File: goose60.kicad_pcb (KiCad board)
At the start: 2 copper layers, 285 x 94.6 mm, 188 parts, among them J1 Debugger, J2 USART, J3 SPI, J4 USB_C_Receptacle_USB2.0, Q1 Q_NMOS_GSD, SW1 SW_Push, SW10 SW_Push, SW11 SW_Push, SW14 SW_Push, SW15 SW_Push, SW16 SW_Push, SW18 SW_Push, SW2 SW_Push, SW20 SW_Push, SW21 SW_Push, SW22 SW_Push, SW23 SW_Push, SW24 SW_Push, SW25 SW_Push, SW26 SW_Push, SW27 SW_Push, SW28 SW_Push, SW29 SW_Push, SW3 SW_Push, SW30 SW_Push, SW31 SW_Push, SW32 SW_Push, SW35 SW_Push, SW36 SW_Push, SW37 SW_Push, SW38 SW_Push, SW39 SW_Push, SW40 SW_Push, SW41 SW_Push, SW42 SW_Push, SW43 SW_Push, SW44 SW_Push, SW45 SW_Push, SW46 SW_Push, SW47 SW_Push, SW48 SW_Push, SW49 SW_Push, SW5 SW_Push, SW50 SW_Push, SW51 SW_Push, SW52 SW_Push, SW53 SW_Push, SW54 SW_Push, SW56 SW_Push, SW58 SW_Push, SW59 SW_Push, SW60 SW_Push, SW61 SW_Push, SW62 SW_Push, SW65 SW_Push, SW66 SW_Push, SW67 SW_Push, SW68 SW_Push, SW69 SW_Push, SW7 SW_Push, SW71 SW_Push, SW73 SW_Push, SW74 SW_Push, SW75 SW_Push, SW76 SW_Push, SW78 SW_Push, SW79 SW_Push, SW80 SW_Push, SW82 SW_Push, SW84 SW_Push, SW86 SW_Push, SW9 SW_Push, U1 STM32F103CBTx, U2 LM317_SOT-223, U3 USBLC6-2SC6, X1 Crystal_GND24

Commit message: fix usb type-c location
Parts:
- moved H7 0.95 mm to (82.0, 73.9)
- moved J4 0.85 mm to (80.7, 67.3)
- moved H8 0.81 mm to (79.3, 73.8)
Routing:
- net Net-(J4-PadA7): track 31.0 -> 30.0 mm
- net row1: track 353.6 -> 354.5 mm
- net Net-(J4-PadB5): track 9.05 -> 9.90 mm
- net Net-(J4-PadA5): track 8.58 -> 9.43 mm
- net Net-(J4-PadA6): track 29.9 -> 29.2 mm

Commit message: change Diode direction and update PR #1 footprint
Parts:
- removed D69: 6.3V/100V, Diode_SMD:D_0603_1608Metric
- added C12: 100uF/16v, Capacitor_SMD:C_1206_3216Metric, B.Cu at (121.3, 85.6)
- added C13: 1uF/16v, Capacitor_SMD:C_0603_1608Metric, B.Cu at (124.8, 84.5)
- added C14: 1uF/16v, Capacitor_SMD:C_0603_1608Metric, B.Cu at (142.3, 85.3)
- added D13: 1N4148, Diode_SMD:D_0805_2012Metric, B.Cu at (139.1, 84.4)
- added R23: 100K/5%, Resistor_SMD:R_0603_1608Metric, B.Cu at (228.6, 144.9)
- added R27: 100K/5%, Resistor_SMD:R_0603_1608Metric, B.Cu at (241.1, 144.9)
- added R28: 10K/5%, Resistor_SMD:R_0603_1608Metric, B.Cu at (117.8, 83.0)
- C1, C2: value 22pF -> 22pF/50V
- C10: footprint Capacitor_SMD:C_0603_1608Metric -> Capacitor_SMD:C_1206_3216Metric
- C3: value 1uF -> 1uF/16V
- C4, C5, C6, C7: value 100nF -> 100nF/16V
- C9: footprint Capacitor_SMD:C_0603_1608Metric -> Capacitor_SMD:C_0805_2012Metric
- D10, D11, D12, D14, D15, D16, D17, D18, D19, D20, D21, D22, D23, D24, D25, D26, D27, D28, D29, D30, D31, D32, D33, D34, D35, D36, D37, D38, D39, D4, D40, D41, D42, D43, D44, D45, D46, D47, D49, D5, D50, D51, D52, D53, D54, D55, D56, D57, D58, D59, D6, D60, D61, D62, D63, D64, D65, D66, D67, D68, D7, D8, D9: footprint Diode_SMD:D_0603_1608Metric -> Diode_SMD:D_0805_2012Metric
- D70: value 1SS355TE -> 1N4148; footprint Diode_SMD:D_0603_1608Metric -> Diode_SMD:D_0805_2012Metric
- R1, R15, R16, R17, R18, R19, R2, R20, R21, R22, R7, R8: value 10K -> 10K/5%
- R10, R9: value 22 -> 22R/5%
- R11: value 1.5K -> 1.5K/5%
- R12, R13, R14: value 0 -> 0R/5%
- R24, R25: value 5.1K -> 5.1K/5%
- R26: value 10K -> 100R/5%
- R3: value 300 -> 330R/5%
- moved C10 1.57 mm to (140.6, 87.8)
- moved D5 0.95 mm to (77.6, 127.4), turned to 180 degrees
- moved D16 0.65 mm to (117.0, 103.1), turned to 180 degrees
- moved D20 0.44 mm to (132.1, 102.3), turned to 90 degrees
- moved D70 0.36 mm to (127.3, 88.0)
- moved D10 0.36 mm to (83.6, 75.8), turned to -90 degrees
- moved D26 0.35 mm to (145.8, 129.3), turned to -90 degrees
- moved D31 0.35 mm to (163.6, 129.3), turned to -90 degrees
- moved D35 0.35 mm to (183.4, 129.3), turned to -90 degrees
- moved D39 0.35 mm to (201.8, 129.3), turned to -90 degrees
- moved D43 0.35 mm to (220.8, 129.3), turned to -90 degrees
- moved D47 0.35 mm to (239.8, 129.3), turned to -90 degrees
- moved D53 0.35 mm to (259.6, 129.3), turned to -90 degrees
- moved D58 0.35 mm to (278.3, 129.3), turned to -90 degrees
- moved D18 0.33 mm to (105.0, 129.3), turned to -90 degrees
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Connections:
- D10 pad 1: Net-(D10-Pad1) -> row1
- D10 pad 2: row1 -> Net-(D10-Pad2)
- D11 pad 1: Net-(D11-Pad1) -> row2
- D11 pad 2: row2 -> Net-(D11-Pad2)
- D12 pad 1: Net-(D12-Pad1) -> row3
- D12 pad 2: row3 -> Net-(D12-Pad2)
- D14 pad 1: Net-(D14-Pad1) -> row5
- D14 pad 2: row5 -> Net-(D14-Pad2)
- D15 pad 1: Net-(D15-Pad1) -> row1
- D15 pad 2: row1 -> Net-(D15-Pad2)
- D16 pad 1: Net-(D16-Pad1) -> row2
- D16 pad 2: row2 -> Net-(D16-Pad2)
- D17 pad 1: Net-(D17-Pad1) -> row3
- D17 pad 2: row3 -> Net-(D17-Pad2)
- D18 pad 1: Net-(D18-Pad1) -> row4
- D18 pad 2: row4 -> Net-(D18-Pad2)
- D19 pad 1: Net-(D19-Pad1) -> row1
- D19 pad 2: row1 -> Net-(D19-Pad2)
- D20 pad 1: Net-(D20-Pad1) -> row2
- D20 pad 2: row2 -> Net-(D20-Pad2)
- D21 pad 1: Net-(D21-Pad1) -> row3
- D21 pad 2: row3 -> Net-(D21-Pad2)
- D22 pad 1: Net-(D22-Pad1) -> row4
- D22 pad 2: row4 -> Net-(D22-Pad2)
- D23 pad 1: Net-(D23-Pad1) -> row1
- D23 pad 2: row1 -> Net-(D23-Pad2)
- D24 pad 1: Net-(D24-Pad1) -> row2
- D24 pad 2: row2 -> Net-(D24-Pad2)
- D25 pad 1: Net-(D25-Pad1) -> row3
- D25 pad 2: row3 -> Net-(D25-Pad2)
- D26 pad 1: Net-(D26-Pad1) -> row4
- D26 pad 2: row4 -> Net-(D26-Pad2)
- D27 pad 1: Net-(D27-Pad1) -> row5
- D27 pad 2: row5 -> Net-(D27-Pad2)
- D28 pad 1: Net-(D28-Pad1) -> row1
- D28 pad 2: row1 -> Net-(D28-Pad2)
- D29 pad 1: Net-(D29-Pad1) -> row2
- D29 pad 2: row2 -> Net-(D29-Pad2)
- D30 pad 1: Net-(D30-Pad1) -> row3
- D30 pad 2: row3 -> Net-(D30-Pad2)
- D31 pad 1: Net-(D31-Pad1) -> row4
- D31 pad 2: row4 -> Net-(D31-Pad2)
- D32 pad 1: Net-(D32-Pad1) -> row1
- D32 pad 2: row1 -> Net-(D32-Pad2)
- D33 pad 1: Net-(D33-Pad1) -> row2
- D33 pad 2: row2 -> Net-(D33-Pad2)
- D34 pad 1: Net-(D34-Pad1) -> row3
- D34 pad 2: row3 -> Net-(D34-Pad2)
- D35 pad 1: Net-(D35-Pad1) -> row4
- D35 pad 2: row4 -> Net-(D35-Pad2)
- D37 pad 1: Net-(D37-Pad1) -> row2
- D37 pad 2: row2 -> Net-(D37-Pad2)
- D38 pad 1: Net-(D38-Pad1) -> row3
- D38 pad 2: row3 -> Net-(D38-Pad2)
- D39 pad 1: Net-(D39-Pad1) -> row4
- D39 pad 2: row4 -> Net-(D39-Pad2)
- D4 pad 1: Net-(D4-Pad1) -> row3
- D4 pad 2: row3 -> Net-(D4-Pad2)
- D40 pad 1: Net-(D40-Pad1) -> row1
- D40 pad 2: row1 -> Net-(D40-Pad2)
- D41 pad 1: Net-(D41-Pad1) -> row2
- D41 pad 2: row2 -> Net-(D41-Pad2)
- D42 pad 1: Net-(D42-Pad1) -> row3
- D42 pad 2: row3 -> Net-(D42-Pad2)
- D43 pad 1: Net-(D43-Pad1) -> row4
- D43 pad 2: row4 -> Net-(D43-Pad2)
- D44 pad 1: Net-(D44-Pad1) -> row1
- D44 pad 2: row1 -> Net-(D44-Pad2)
- D45 pad 1: Net-(D45-Pad1) -> row2
- D45 pad 2: row2 -> Net-(D45-Pad2)
- D46 pad 1: Net-(D46-Pad1) -> row3
- D46 pad 2: row3 -> Net-(D46-Pad2)
- D47 pad 1: Net-(D47-Pad1) -> row4
- D47 pad 2: row4 -> Net-(D47-Pad2)
- D49 pad 1: Net-(D49-Pad1) -> row5
- D49 pad 2: row5 -> Net-(D49-Pad2)
- D5 pad 1: Net-(D5-Pad1) -> row4
- D5 pad 2: row4 -> Net-(D5-Pad2)
- D50 pad 1: Net-(D50-Pad1) -> row1
- D50 pad 2: row1 -> Net-(D50-Pad2)
- D51 pad 1: Net-(D51-Pad1) -> row2
- D51 pad 2: row2 -> Net-(D51-Pad2)
- D52 pad 1: Net-(D52-Pad1) -> row3
- D52 pad 2: row3 -> Net-(D52-Pad2)
- D53 pad 1: Net-(D53-Pad1) -> row4
- D53 pad 2: row4 -> Net-(D53-Pad2)
- D54 pad 1: Net-(D54-Pad1) -> row5
- D54 pad 2: row5 -> Net-(D54-Pad2)
- D55 pad 1: Net-(D55-Pad1) -> row1
- D55 pad 2: row1 -> Net-(D55-Pad2)
- D56 pad 1: Net-(D56-Pad1) -> row2
- D56 pad 2: row2 -> Net-(D56-Pad2)
- D57 pad 1: Net-(D57-Pad1) -> row3
- D57 pad 2: row3 -> Net-(D57-Pad2)
- D58 pad 1: Net-(D58-Pad1) -> row4
- D58 pad 2: row4 -> Net-(D58-Pad2)
- D59 pad 1: Net-(D59-Pad1) -> row4
- D59 pad 2: row4 -> Net-(D59-Pad2)
- D6 pad 1: Net-(D6-Pad1) -> row5
- D6 pad 2: row5 -> Net-(D6-Pad2)
- D60 pad 1: Net-(D60-Pad1) -> row5
- D60 pad 2: row5 -> Net-(D60-Pad2)
- D61 pad 1: Net-(D61-Pad1) -> row1
- D61 pad 2: row1 -> Net-(D61-Pad2)
- D62 pad 1: Net-(D62-Pad1) -> row2
- D62 pad 2: row2 -> Net-(D62-Pad2)
- D63 pad 1: Net-(D63-Pad1) -> row3
- D63 pad 2: row3 -> Net-(D63-Pad2)
- D64 pad 1: Net-(D64-Pad1) -> row3
- D64 pad 2: row3 -> Net-(D64-Pad2)
- D65 pad 1: Net-(D65-Pad1) -> row4
- D65 pad 2: row4 -> Net-(D65-Pad2)
- D66 pad 1: Net-(D66-Pad1) -> row5
- D66 pad 2: row5 -> Net-(D66-Pad2)
- D67 pad 1: Net-(D67-Pad1) -> row1
- D67 pad 2: row1 -> Net-(D67-Pad2)
- D68 pad 1: Net-(D68-Pad1) -> row2
- D68 pad 2: row2 -> Net-(D68-Pad2)
- D7 pad 1: Net-(D7-Pad1) -> row1
- D7 pad 2: row1 -> Net-(D7-Pad2)
- D8 pad 1: Net-(D8-Pad1) -> row2
- D8 pad 2: row2 -> Net-(D8-Pad2)
- D9 pad 1: Net-(D9-Pad1) -> row5
- D9 pad 2: row5 -> Net-(D9-Pad2)
- R1 pad 2: BOOT0 -> Net-(R1-Pad2)
- SW1 pad 1: GND -> BOOT0
- SW1 pad 2: BOOT0 -> Net-(R1-Pad2)
- SW10 pad 1: Net-(D8-Pad1) -> Net-(D8-Pad2)
- SW11 pad 1: Net-(D9-Pad1) -> Net-(D9-Pad2)
- SW14 pad 1: Net-(D10-Pad1) -> Net-(D10-Pad2)
- SW15 pad 1: Net-(D11-Pad1) -> Net-(D11-Pad2)
- SW16 pad 1: Net-(D12-Pad1) -> Net-(D12-Pad2)
- SW18 pad 1: Net-(D14-Pad1) -> Net-(D14-Pad2)
- SW2 pad 1: GND -> Net-(R27-Pad1)
- SW20 pad 1: Net-(D15-Pad1) -> Net-(D15-Pad2)
- SW21 pad 1: Net-(D16-Pad1) -> Net-(D16-Pad2)
- SW22 pad 1: Net-(D17-Pad1) -> Net-(D17-Pad2)
- SW23 pad 1: Net-(D18-Pad1) -> Net-(D18-Pad2)
- SW24 pad 1: Net-(D19-Pad1) -> Net-(D19-Pad2)
- SW25 pad 1: Net-(D20-Pad1) -> Net-(D20-Pad2)
- SW26 pad 1: Net-(D21-Pad1) -> Net-(D21-Pad2)
- SW27 pad 1: Net-(D22-Pad1) -> Net-(D22-Pad2)
- SW28 pad 1: Net-(D23-Pad1) -> Net-(D23-Pad2)
- SW29 pad 1: Net-(D24-Pad1) -> Net-(D24-Pad2)
- SW3 pad 1: Net-(D4-Pad1) -> Net-(D4-Pad2)
- SW30 pad 1: Net-(D25-Pad1) -> Net-(D25-Pad2)
- SW31 pad 1: Net-(D26-Pad1) -> Net-(D26-Pad2)
- SW32 pad 1: Net-(D27-Pad1) -> Net-(D27-Pad2)
- SW35 pad 1: Net-(D28-Pad1) -> Net-(D28-Pad2)
- SW36 pad 1: Net-(D29-Pad1) -> Net-(D29-Pad2)
- SW37 pad 1: Net-(D30-Pad1) -> Net-(D30-Pad2)
- SW38 pad 1: Net-(D31-Pad1) -> Net-(D31-Pad2)
- SW39 pad 1: Net-(D32-Pad1) -> Net-(D32-Pad2)
- SW40 pad 1: Net-(D33-Pad1) -> Net-(D33-Pad2)
- SW41 pad 1: Net-(D34-Pad1) -> Net-(D34-Pad2)
- SW42 pad 1: Net-(D35-Pad1) -> Net-(D35-Pad2)
- SW44 pad 1: Net-(D37-Pad1) -> Net-(D37-Pad2)
- SW45 pad 1: Net-(D38-Pad1) -> Net-(D38-Pad2)
- SW46 pad 1: Net-(D39-Pad1) -> Net-(D39-Pad2)
- SW47 pad 1: Net-(D40-Pad1) -> Net-(D40-Pad2)
- SW48 pad 1: Net-(D41-Pad1) -> Net-(D41-Pad2)
- SW49 pad 1: Net-(D42-Pad1) -> Net-(D42-Pad2)
- SW5 pad 1: Net-(D5-Pad1) -> Net-(D5-Pad2)
- SW50 pad 1: Net-(D43-Pad1) -> Net-(D43-Pad2)
- SW51 pad 1: Net-(D44-Pad1) -> Net-(D44-Pad2)
- SW52 pad 1: Net-(D45-Pad1) -> Net-(D45-Pad2)
- SW53 pad 1: Net-(D46-Pad1) -> Net-(D46-Pad2)
- SW54 pad 1: Net-(D47-Pad1) -> Net-(D47-Pad2)
- SW56 pad 1: Net-(D49-Pad1) -> Net-(D49-Pad2)
- SW58 pad 1: Net-(D50-Pad1) -> Net-(D50-Pad2)
- SW59 pad 1: Net-(D51-Pad1) -> Net-(D51-Pad2)
- SW60 pad 1: Net-(D52-Pad1) -> Net-(D52-Pad2)
- SW61 pad 1: Net-(D53-Pad1) -> Net-(D53-Pad2)
- SW62 pad 1: Net-(D54-Pad1) -> Net-(D54-Pad2)
- SW65 pad 1: Net-(D55-Pad1) -> Net-(D55-Pad2)
- SW66 pad 1: Net-(D56-Pad1) -> Net-(D56-Pad2)
- SW67 pad 1: Net-(D57-Pad1) -> Net-(D57-Pad2)
- SW68 pad 1: Net-(D58-Pad1) -> Net-(D58-Pad2)
- SW69 pad 1: Net-(D59-Pad1) -> Net-(D59-Pad2)
- SW7 pad 1: Net-(D6-Pad1) -> Net-(D6-Pad2)
- SW71 pad 1: Net-(D60-Pad1) -> Net-(D60-Pad2)
- SW73 pad 1: Net-(D61-Pad1) -> Net-(D61-Pad2)
- SW74 pad 1: Net-(D62-Pad1) -> Net-(D62-Pad2)
- SW75 pad 1: Net-(D63-Pad1) -> Net-(D63-Pad2)
- SW76 pad 1: Net-(D64-Pad1) -> Net-(D64-Pad2)
- SW78 pad 1: Net-(D64-Pad1) -> Net-(D64-Pad2)
- SW79 pad 1: Net-(D65-Pad1) -> Net-(D65-Pad2)
- SW80 pad 1: Net-(D65-Pad1) -> Net-(D65-Pad2)
- SW82 pad 1: Net-(D67-Pad1) -> Net-(D67-Pad2)
- SW84 pad 1: Net-(D66-Pad1) -> Net-(D66-Pad2)
- SW86 pad 1: Net-(D68-Pad1) -> Net-(D68-Pad2)
- SW9 pad 1: Net-(D7-Pad1) -> Net-(D7-Pad2)
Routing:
- net GND: track 433.8 -> 509.8 mm, vias 18 -> 20
- net Net-(D64-Pad1): track 18.4 -> 0.00 mm
- net Net-(D64-Pad2): track 0.00 -> 18.4 mm
- net Net-(D65-Pad1): track 15.3 -> 0.00 mm
- net Net-(D65-Pad2): track 0.00 -> 15.0 mm
- net Net-(D6-Pad1): track 14.8 -> 0.00 mm
- net Net-(D63-Pad1): track 14.7 -> 0.00 mm
- net Net-(D6-Pad2): track 0.00 -> 14.7 mm
- net Net-(D63-Pad2): track 0.00 -> 14.4 mm
- net Net-(D59-Pad1): track 13.2 -> 0.00 mm
- net Net-(D59-Pad2): track 0.00 -> 13.2 mm
- net VIN: track 85.4 -> 97.4 mm
- net row3: track 324.8 -> 335.5 mm
- net Net-(D5-Pad1): track 9.59 -> 0.00 mm
- net Net-(D5-Pad2): track 0.00 -> 9.51 mm
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
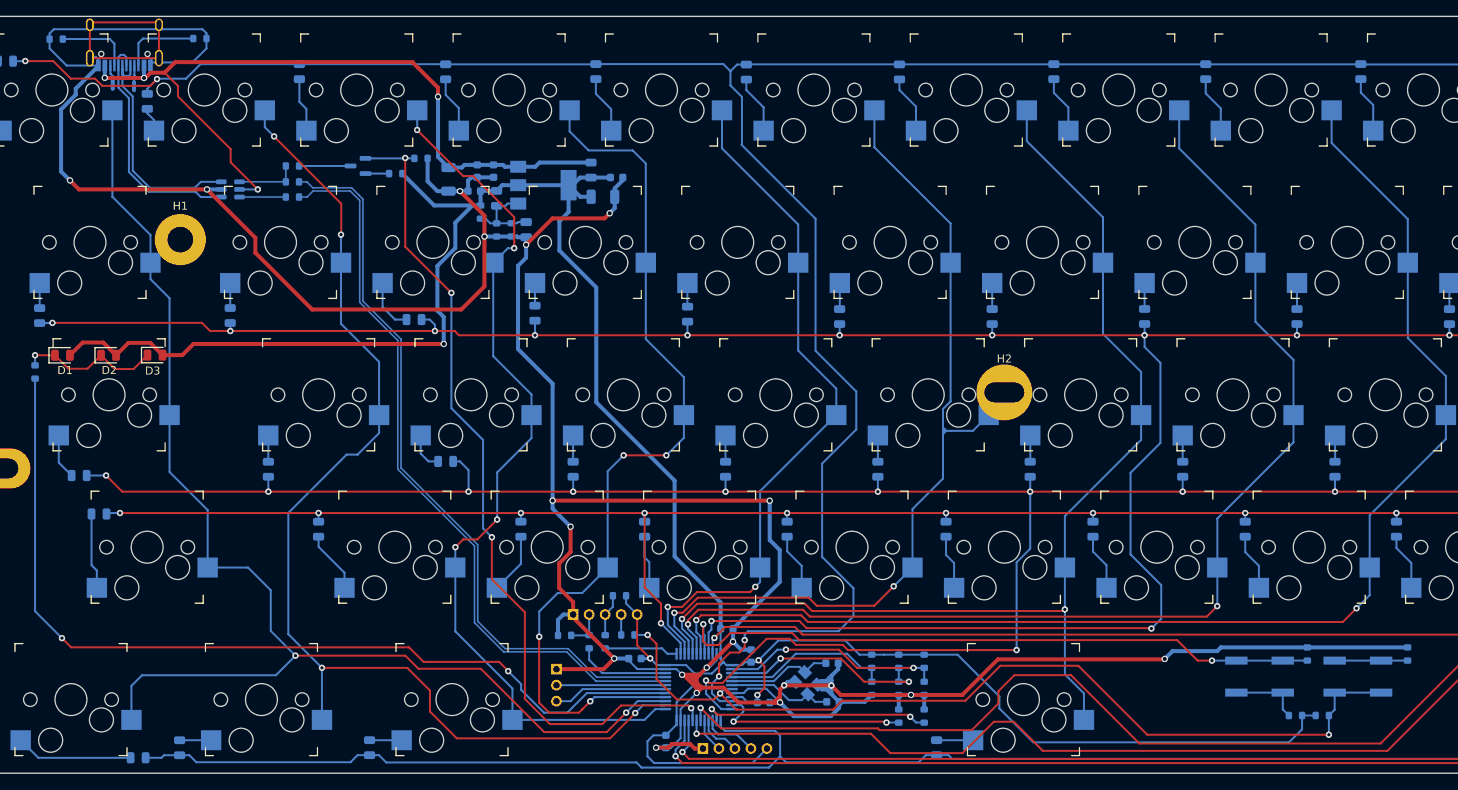
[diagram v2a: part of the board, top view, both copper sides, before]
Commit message: fix layout rule error and warring
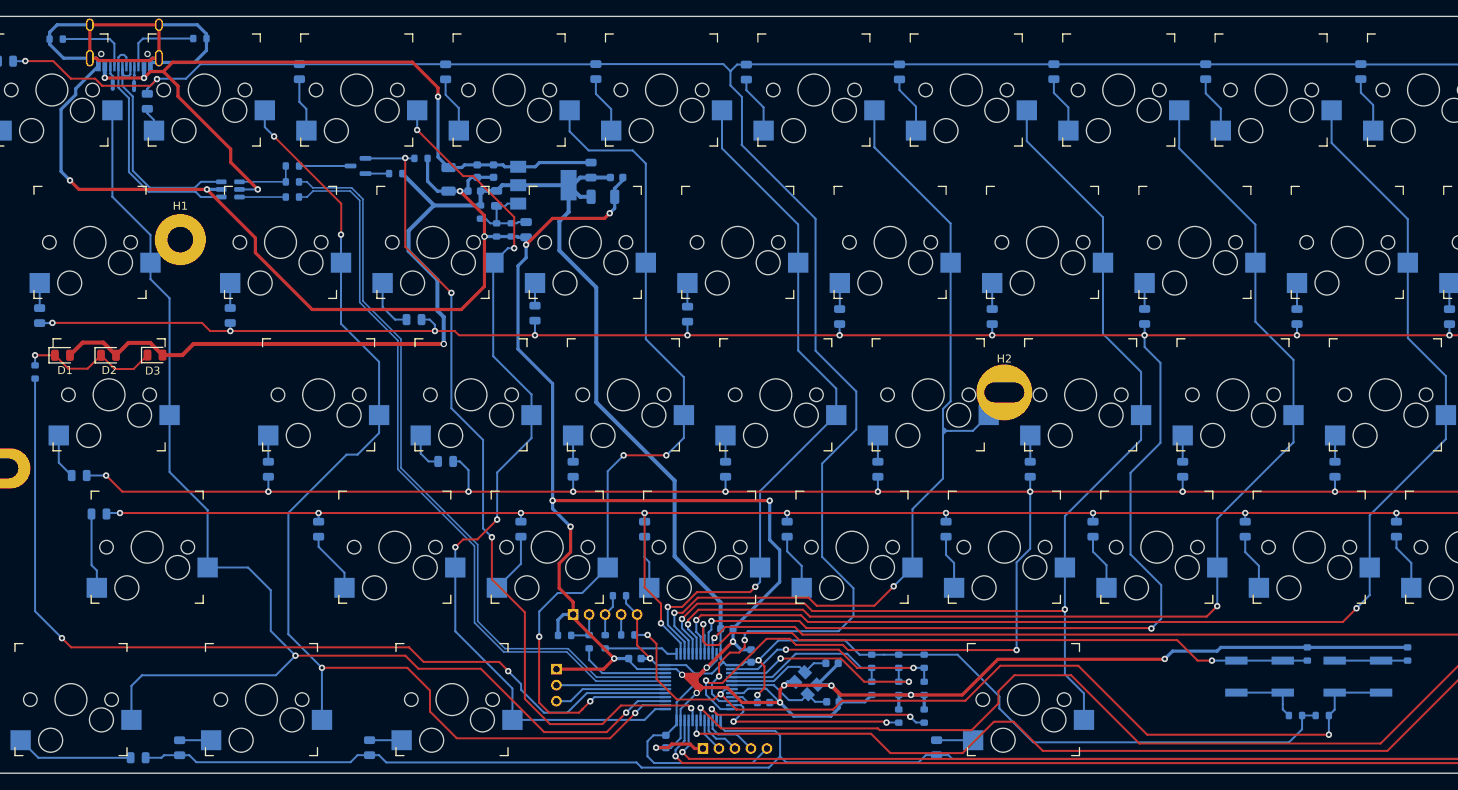
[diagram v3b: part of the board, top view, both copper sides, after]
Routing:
- net GND: track 509.8 -> 488.1 mm
